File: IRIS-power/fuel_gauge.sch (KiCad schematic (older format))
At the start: 9 parts, among them Q21 2N7002, U21 MAX17261

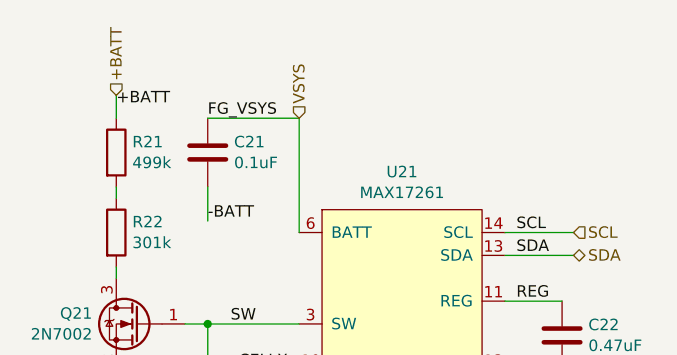
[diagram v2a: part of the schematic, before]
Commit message: Updated layout
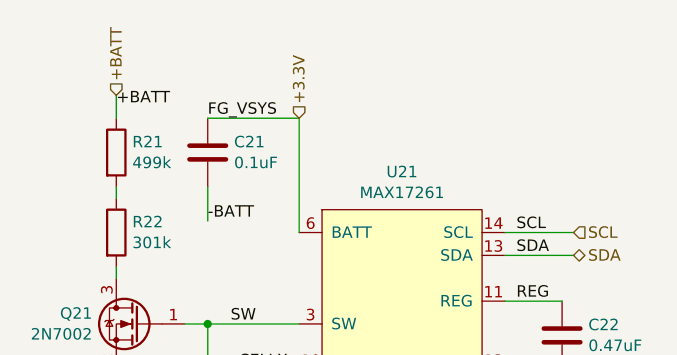
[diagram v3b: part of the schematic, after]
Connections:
- net VSYS renamed +3.3V
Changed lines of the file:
@@
 SDA
 Text HLabel 5800 3100 1    50   Input ~ 0
-VSYS
++3.3V
 Wire Wire Line
 	5000 4200 5800 4200

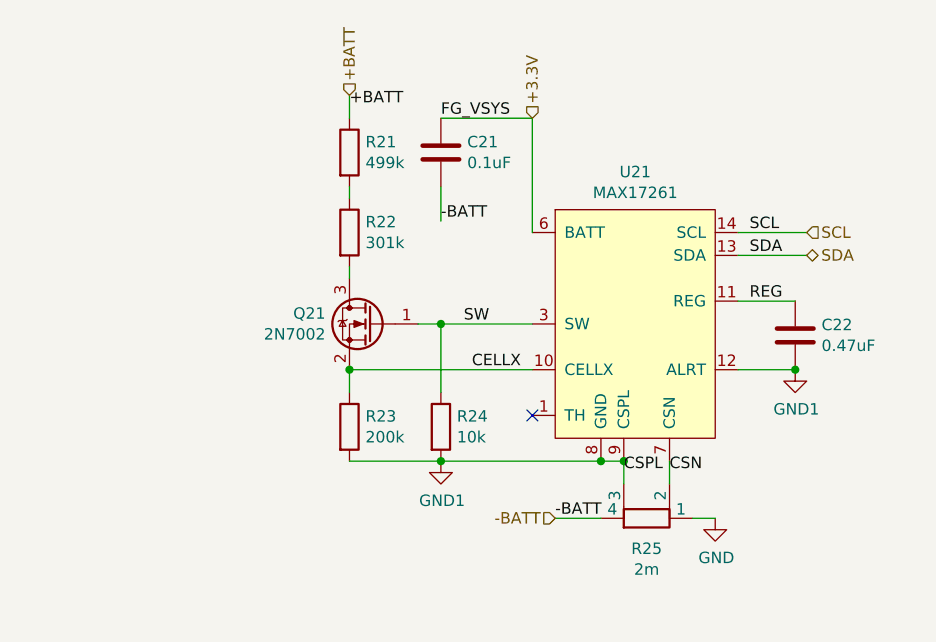
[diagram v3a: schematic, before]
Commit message: Improved fuel gauge layout
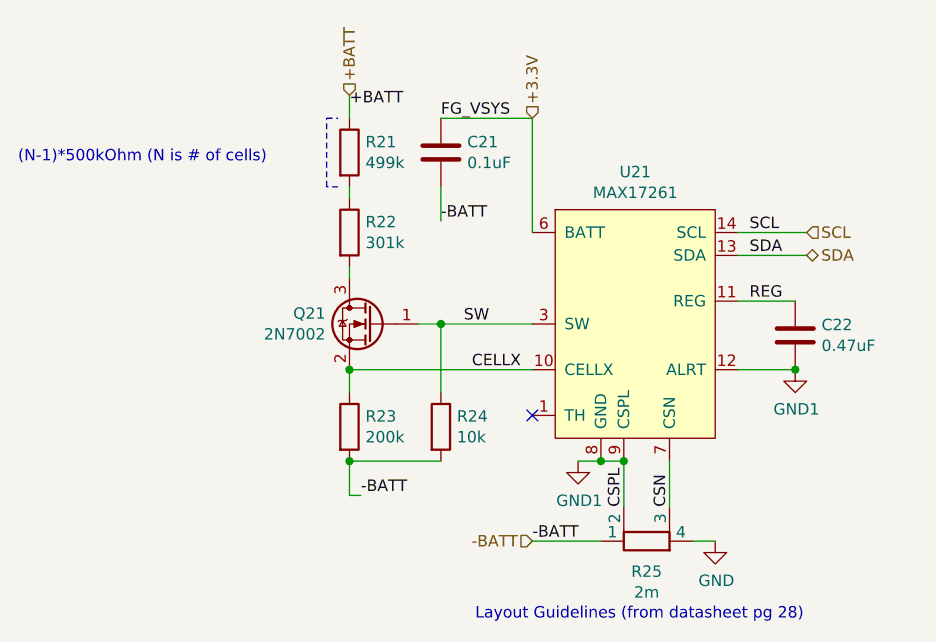
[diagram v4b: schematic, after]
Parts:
- C21: Digikey PN (none) -> 1276-CL10B104KB8NNNLCT-ND
- C22: Digikey PN (none) -> 587-3506-1-ND
- Q21: Digikey PN (none) -> 1727-8643-1-ND
- R24: Digikey PN (none) -> RNCP0603FTD10K0CT-ND
- U21: Digikey PN (none) -> 175-MAX17261METD+TCT-ND
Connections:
- net -BATT: now also R23.2, R24.2, R25.1; no longer R25.4
- net CSN: now also R25.3; no longer R25.2
- net GND: now also R25.4; no longer R25.1
- net GND1: now also R25.2; no longer R23.2, R24.2, R25.3
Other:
- note added: "(N-1)*500kOhm (N is # of cells)"
- note added: "Layout Guidelines (from datasheet pg 28)\n"
- moved on the sheet: R25
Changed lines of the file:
@@
 L power:GND1 #PWR?
 U 1 1 5F3ED548
-P 5400 4600
+P 6000 4600
 AR Path="/5F3ED548" Ref="#PWR?"  Part="1"
 AR Path="/5F3CDA08/5F3ED548" Ref="#PWR021"  Part="1"
-F 0 "#PWR021" H 5400 4350 50  0001 C CNN
-F 1 "GND1" H 5405 4427 50  0000 C CNN
-F 2 "" H 5400 4600 50  0001 C CNN
-F 3 "" H 5400 4600 50  0001 C CNN
-	1    5400 4600
+F 0 "#PWR021" H 6000 4350 50  0001 C CNN
+F 1 "GND1" H 6005 4427 50  0000 C CNN
+F 2 "" H 6000 4600 50  0001 C CNN
+F 3 "" H 6000 4600 50  0001 C CNN
+	1    6000 4600
 	1    0    0    -1
 $EndComp
@@
 L power:GND #PWR?
 U 1 1 5F3ED567
-P 6600 4850
+P 6600 4950
 AR Path="/5F3ED567" Ref="#PWR?"  Part="1"
 AR Path="/5F3CDA08/5F3ED567" Ref="#PWR022"  Part="1"
-F 0 "#PWR022" H 6600 4600 50  0001 C CNN
-F 1 "GND" H 6605 4677 50  0000 C CNN
-F 2 "" H 6600 4850 50  0001 C CNN
-F 3 "" H 6600 4850 50  0001 C CNN
-	1    6600 4850
+F 0 "#PWR022" H 6600 4700 50  0001 C CNN
+F 1 "GND" H 6605 4777 50  0000 C CNN
+F 2 "" H 6600 4950 50  0001 C CNN
+F 3 "" H 6600 4950 50  0001 C CNN
+	1    6600 4950
 	1    0    0    -1
 $EndComp
@@
 F 2 "Resistor_SMD:R_0603_1608Metric" V 5330 4450 50  0001 C CNN
 F 3 "~" H 5400 4450 50  0001 C CNN
+F 4 "RNCP0603FTD10K0CT-ND" H 5400 4450 50  0001 C CNN "Digikey PN"
 	1    5400 4450
 	1    0    0    -1
@@
 F 2 "Capacitor_SMD:C_0603_1608Metric" H 5438 3100 50  0001 C CNN
 F 3 "~" H 5400 3250 50  0001 C CNN
+F 4 "1276-CL10B104KB8NNNLCT-ND" H 5400 3250 50  0001 C CNN "Digikey PN"
 	1    5400 3250
 	1    0    0    -1
@@
 F 2 "Capacitor_SMD:C_0603_1608Metric" H 6988 3900 50  0001 C CNN
 F 3 "~" H 6950 4050 50  0001 C CNN
+F 4 "587-3506-1-ND" H 6950 4050 50  0001 C CNN "Digikey PN"
 	1    6950 4050
 	1    0    0    -1
@@
 F 2 "Package_TO_SOT_SMD:SOT-23" H 5300 3925 50  0001 L CIN
 F 3 "https://www.fairchildsemi.com/datasheets/2N/2N7002.pdf" H 5100 4000 50  0001 L CNN
+F 4 "1727-8643-1-ND" H 5100 4000 50  0001 C CNN "Digikey PN"
 	1    5100 4000
 	-1   0    0    -1
 $EndComp
-Wire Wire Line
-	6400 4700 6400 4600
-Wire Wire Line
-	6200 4700 6200 4600
 $Comp
 L Device:R_Shunt R?
 U 1 1 5F3ED5AE
-P 6300 4850
+P 6300 4950
 AR Path="/5F3ED5AE" Ref="R?"  Part="1"
 AR Path="/5F3CDA08/5F3ED5AE" Ref="R25"  Part="1"
-F 0 "R25" V 6167 4850 50  0000 C CNN
-F 1 "2m" V 6076 4850 50  0000 C CNN
-F 2 "star-common-lib:CST0612-FC-R002E" V 6230 4850 50  0001 C CNN
-F 3 "https://www.bourns.com/docs/product-datasheets/cst0612.pdf" H 6300 4850 50  0001 C CNN
-F 4 "CST0612-FC-R002ECT-ND" H 6300 4850 50  0001 C CNN "Digikey PN"
-F 5 "CST0612-FC-R002E" H 6300 4850 50  0001 C CNN "MFG PN"
-F 6 "0.78" H 6300 4850 50  0001 C CNN "Unit Cost"
-	1    6300 4850
-	0    1    -1   0
+F 0 "R25" V 6167 4950 50  0000 C CNN
+F 1 "2m" V 6076 4950 50  0000 C CNN
+F 2 "star-common-lib:CST0612-FC-R002E" V 6230 4950 50  0001 C CNN
+F 3 "https://www.bourns.com/docs/product-datasheets/cst0612.pdf" H 6300 4950 50  0001 C CNN
+F 4 "CST0612-FC-R002ECT-ND" H 6300 4950 50  0001 C CNN "Digikey PN"
+F 5 "CST0612-FC-R002E" H 6300 4950 50  0001 C CNN "MFG PN"
+F 6 "0.78" H 6300 4950 50  0001 C CNN "Unit Cost"
+	1    6300 4950
+	0    -1   -1   0
 $EndComp
 Wire Wire Line
@@
 Connection ~ 5000 4200
 Connection ~ 5400 4000
-Connection ~ 5400 4600
 Wire Wire Line
 	5300 4000 5400 4000
@@
 Text HLabel 5000 3000 1    50   Input ~ 0
 +BATT
-Text HLabel 5900 4850 0    50   Input ~ 0
--BATT
-Wire Wire Line
-	6600 4850 6500 4850
+Text HLabel 5800 4950 0    50   Input ~ 0
+-BATT
+Wire Wire Line
+	6600 4950 6500 4950
 Text HLabel 7000 3600 2    50   Input ~ 0
 SCL
@@
 Wire Wire Line
 	6700 4200 6950 4200
-Text Label 6200 4650 0    50   ~ 0
+Text Label 6200 4800 1    50   ~ 0
 CSPL
-Text Label 6400 4650 0    50   ~ 0
+Text Label 6400 4800 1    50   ~ 0
 CSN
 Wire Wire Line
@@
 Text Label 5000 3050 0    50   ~ 0
 +BATT
-Connection ~ 6200 4600
 Wire Wire Line
 	6100 4600 6200 4600
-Connection ~ 6100 4600
 $Comp
 L star-common-lib:MAX17261 U?
@@
 F 2 "star-common-lib:MAX17261" H 6250 4000 50  0001 C CNN
 F 3 "" H 6250 4000 50  0001 C CNN
+F 4 "175-MAX17261METD+TCT-ND" H 6250 4000 50  0001 C CNN "Digikey PN"
 	1    6250 4000
 	1    0    0    -1
 $EndComp
-Wire Wire Line
-	5400 4600 6100 4600
-Wire Wire Line
-	5900 4850 6100 4850
-Text Label 5900 4850 0    50   ~ 0
+Text Label 5800 4950 0    50   ~ 0
 -BATT
 Text Label 5400 3550 0    50   ~ 0
@@
 Text Label 5400 3100 0    50   ~ 0
 FG_VSYS
+Wire Notes Line
+	4950 3400 4900 3400
+Wire Notes Line
+	4900 3400 4900 3100
+Wire Notes Line
+	4900 3100 4950 3100
+Text Notes 3550 3300 0    50   ~ 0
+(N-1)*500kOhm (N is # of cells)
+Text Label 5050 4750 0    50   ~ 0
+-BATT
+Wire Wire Line
+	5050 4750 5000 4750
+Wire Wire Line
+	5000 4750 5000 4600
+Connection ~ 5000 4600
+Wire Wire Line
+	6000 4600 6100 4600
+Connection ~ 6100 4600
+Wire Wire Line
+	6200 4600 6200 4800
+Connection ~ 6200 4600
+Wire Wire Line
+	6400 4600 6400 4800
+Wire Wire Line
+	5800 4950 6100 4950
+Text Notes 5550 5300 0    50   ~ 0
+Layout Guidelines (from datasheet pg 28)\n
 $EndSCHEMATC

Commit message: Adjusted silkscreen
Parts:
- R21: Digikey PN (none) -> 311-2595-1-ND
- R22: Digikey PN (none) -> RR08P301KDCT-ND
- R23: Digikey PN (none) -> RR08P200KDCT-ND
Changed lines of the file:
@@
 F 2 "Resistor_SMD:R_0603_1608Metric" V 4930 3250 50  0001 C CNN
 F 3 "~" H 5000 3250 50  0001 C CNN
+F 4 "311-2595-1-ND" H 5000 3250 50  0001 C CNN "Digikey PN"
 	1    5000 3250
 	1    0    0    -1
@@
 F 2 "Resistor_SMD:R_0603_1608Metric" V 4930 3600 50  0001 C CNN
 F 3 "~" H 5000 3600 50  0001 C CNN
+F 4 "RR08P301KDCT-ND" H 5000 3600 50  0001 C CNN "Digikey PN"
 	1    5000 3600
 	1    0    0    -1
@@
 F 2 "Resistor_SMD:R_0603_1608Metric" V 4930 4450 50  0001 C CNN
 F 3 "~" H 5000 4450 50  0001 C CNN
+F 4 "RR08P200KDCT-ND" H 5000 4450 50  0001 C CNN "Digikey PN"
 	1    5000 4450
 	1    0    0    -1

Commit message: IRIS V4.02
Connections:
- net +3.3V: now also U21.1 (TH)
- no-connect marks 1 -> 0
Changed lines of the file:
@@
 	1    0    0    -1
 $EndComp
-NoConn ~ 5800 4400
 $Comp
 L Device:R R?
@@
 Text Notes 5550 5300 0    50   ~ 0
 Layout Guidelines (from datasheet pg 28)\n
+Wire Wire Line
+	5800 3600 5700 3600
+Wire Wire Line
+	5700 3600 5700 4400
+Wire Wire Line
+	5700 4400 5800 4400
+Connection ~ 5800 3600
 $EndSCHEMATC
